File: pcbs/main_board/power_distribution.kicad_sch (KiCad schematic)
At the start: 23 parts, among them J1 BAT1, J2 BAT2, Q1 PMOS, SW1 Power switch, U5 Step-up, U7 TP4056-42-ESOP8, U8 ST1L08

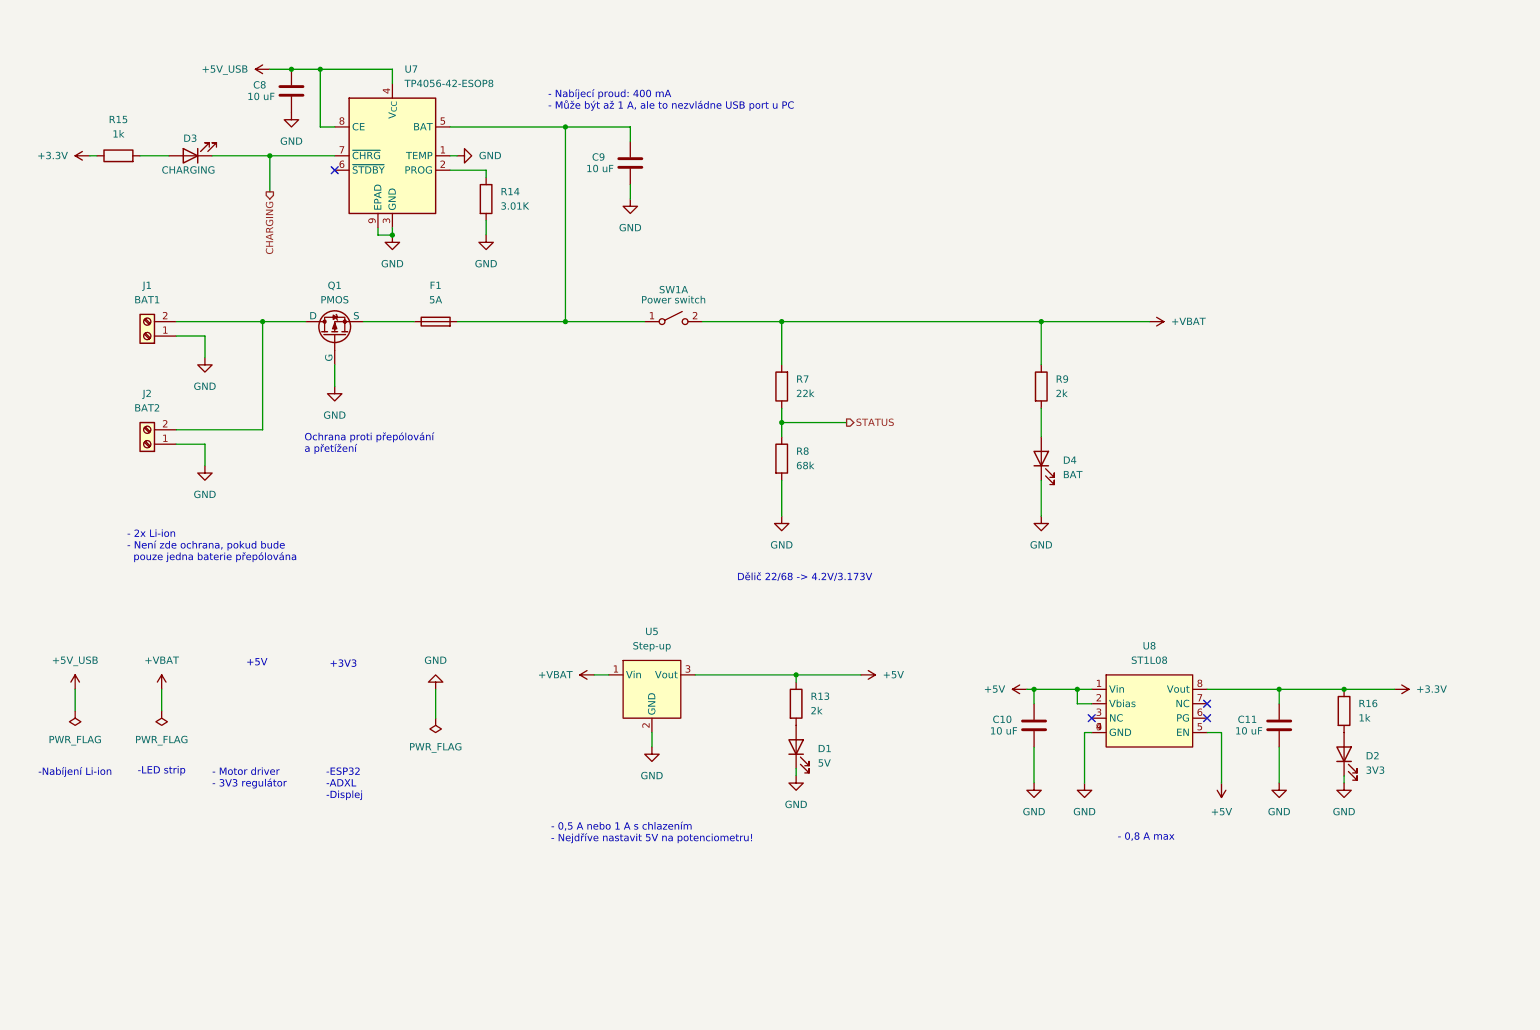
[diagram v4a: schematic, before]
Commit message: Add reverse polarity protection
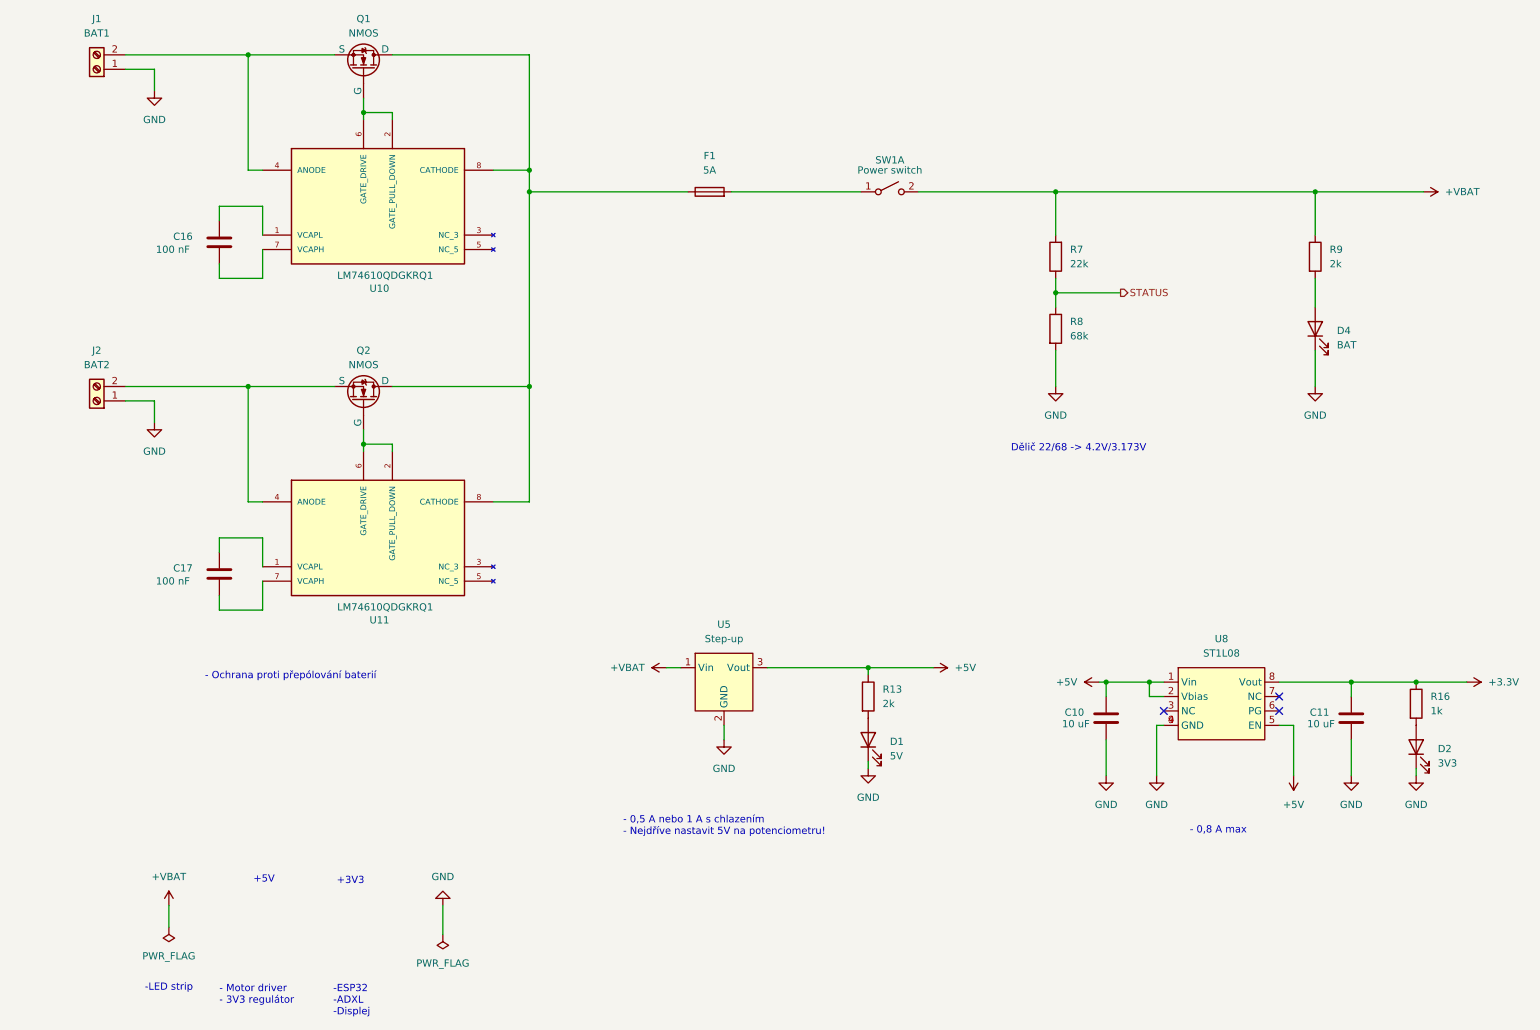
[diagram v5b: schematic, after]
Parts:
- removed C8, C9: 10 uF, Capacitor_SMD:C_0603_1608Metric_Pad1.08x0.95mm_HandSolder, symbol Device:C
- removed D3: CHARGING, LED_SMD:LED_0805_2012Metric_Pad1.15x1.40mm_HandSolder, symbol Device:LED
- removed Q1: PMOS, Package_TO_SOT_SMD:TO-252-2, symbol Simulation_SPICE:PMOS
- removed R14: 3.01K, Resistor_SMD:R_0603_1608Metric_Pad0.98x0.95mm_HandSolder, symbol Device:R
- removed R15: 1k, Resistor_SMD:R_0603_1608Metric_Pad0.98x0.95mm_HandSolder, symbol Device:R
- removed U7: TP4056-42-ESOP8, Package_SO:SOIC-8-1EP_3.9x4.9mm_P1.27mm_EP2.41x3.3mm_ThermalVias, symbol Battery_Management:TP4056-42-ESOP8
- added C16, C17: 100 nF, Capacitor_SMD:C_0603_1608Metric_Pad1.08x0.95mm_HandSolder, symbol Device:C
- added Q1, Q2: NMOS, Package_SO:SO-8_3.9x4.9mm_P1.27mm, symbol Simulation_SPICE:NMOS
- added U10, U11: LM74610QDGKRQ1, LM74610QDGKRQ1:SOP65P490X110-8N, symbol LM74610QDGKRQ1:LM74610QDGKRQ1
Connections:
- net at J1.2 (Pin_2): now also Q1.1 (S), Q1.2 (S), Q1.3 (S), U10.4 (ANODE); no longer J2.2 (Pin_2)
- net at F1.1: now also Q1.5 (D), Q1.6 (D), Q1.7 (D), Q1.8 (D), Q2.5 (D), Q2.6 (D), Q2.7 (D), Q2.8 (D), U10.8 (CATHODE), U11.8 (CATHODE)
- new net: Q1.4 (G), U10.2 (GATE_PULL_DOWN), U10.6 (GATE_DRIVE)
- new net: C17.2, U11.1 (VCAPL)
- new net: Q2.4 (G), U11.2 (GATE_PULL_DOWN), U11.6 (GATE_DRIVE)
- new net: J2.2 (Pin_2), Q2.1 (S), Q2.2 (S), Q2.3 (S), U11.4 (ANODE)
- new net: C17.1, U11.7 (VCAPH)
- new net: C16.1, U10.7 (VCAPH)
- new net: C16.2, U10.1 (VCAPL)
- no-connect marks 4 -> 3
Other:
- note added: "- Ochrana proti přepólování baterií"
- note removed: "- 2x Li-ion - Není zde ochrana, pokud bude pouze jedna baterie přepólována"
- note removed: "- Nabíjecí proud: 400 mA - Může být až 1 A, ale to nezvládne USB port u PC"
- note removed: "-Nabíjení Li-ion"
- note removed: "Ochrana proti přepólování a přetížení"
- moved on the sheet: C10, C11, D1, D2, D4, F1, J1, J2, R13, R16, R7, R8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

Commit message: Components update
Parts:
- U10, U11: Availability In Stock -> (none); Check_prices https://www.snapeda.com/parts/LM74610QDGKRQ1/Texas+Instrume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 -> (none); Description_1 0.48-V to 42-V, zero IQ automotive ideal diode controller -> (none); MANUFACTURER Texas Instruments -> (none); MAXIMUM_PACKAGE_HEIGHT 1.10 mm -> (none); MF Texas Instruments -> (none); MP LM74610QDGKRQ1 -> (none); PARTREV B -> (none); Package VSSOP-8 Texas Instruments -> (none); Price None -> (none); STANDARD IPC-7351B -> (none); SnapEDA_Link https://www.snapeda.com/parts/LM74610QDGKRQ1/Texas+Instrume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 -> (none)

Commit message: Main board final update
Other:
- company: (none) -> Brno Mars Rover
- title: (none) -> Main board - MyMachine LED cap
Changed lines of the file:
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@@
 	(generator_version "9.0")
 	(paper "A4")
+	(title_block
+		(title "Main board - MyMachine LED cap")
+		(date "2026-01-20")
+		(company "Brno Mars Rover")
+	)
 	(text "-ESP32\n-ADXL\n-Displej"
 		(exclude_from_sim no)
